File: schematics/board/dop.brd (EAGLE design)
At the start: 65.8 x 65.8 mm, 72 parts

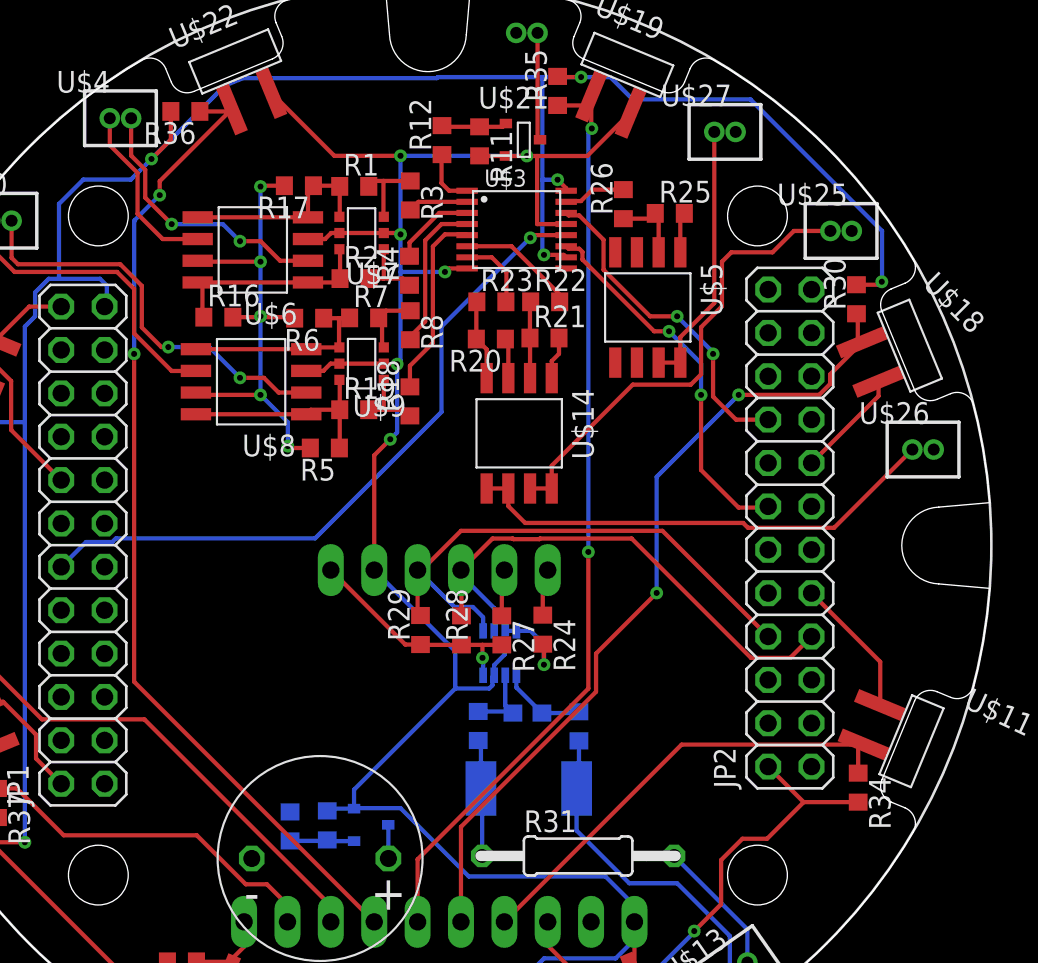
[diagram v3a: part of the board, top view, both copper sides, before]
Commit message: Сделали новую плату для кнопок на нижнем двигателе
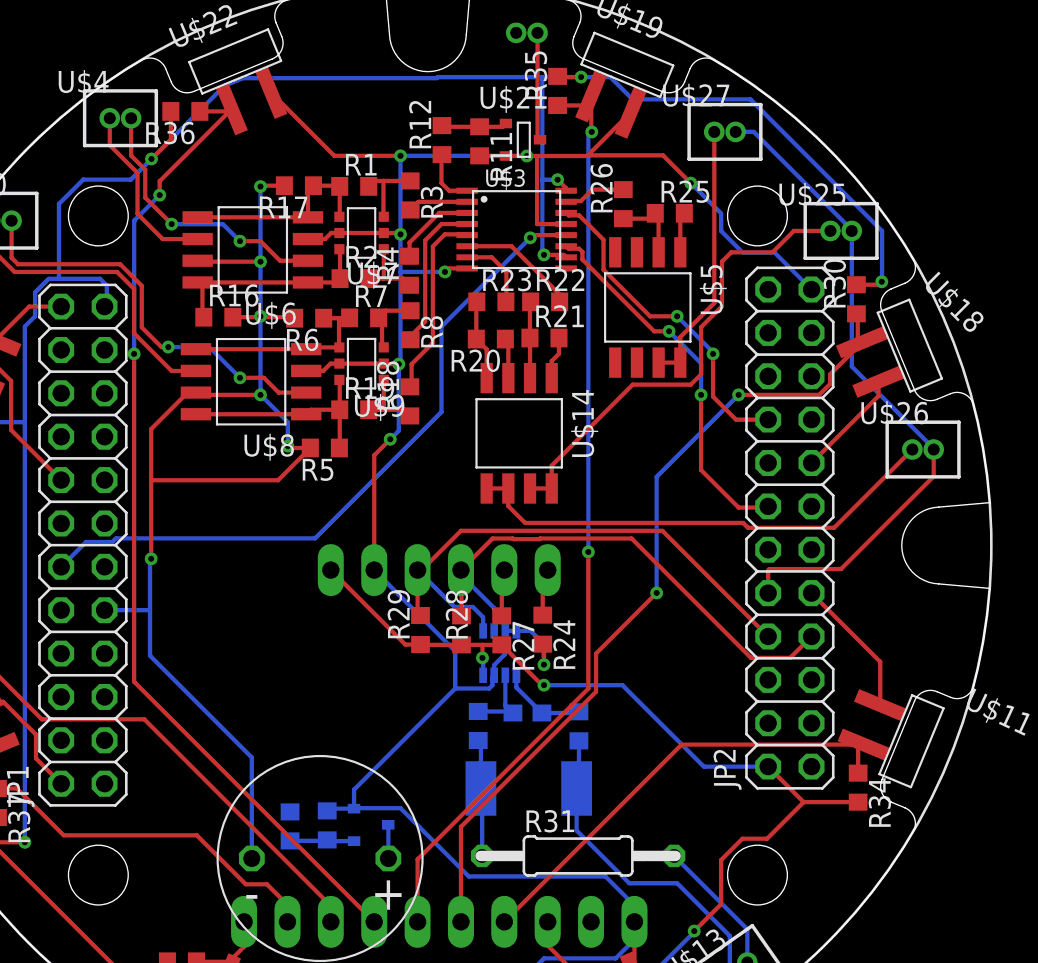
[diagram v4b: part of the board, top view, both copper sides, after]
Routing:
- net 5V: track 30.3 -> 74.2 mm, vias 5 -> 6
- net VAB: track 0.00 -> 38.9 mm
- net 3V3: track 211.5 -> 230.1 mm, vias 12 -> 13
- net GND: track 187.6 -> 204.7 mm, vias 8 -> 9
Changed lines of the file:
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@@
 <?xml version="1.0" encoding="utf-8"?>
 <!DOCTYPE eagle SYSTEM "eagle.dtd">
-<eagle version="9.4.2">
+<eagle version="9.6.2">
 <drawing>
 <settings>
-<setting alwaysvectorfont="yes"/>
+<setting alwaysvectorfont="no"/>
 <setting verticaltext="up"/>
 </settings>
@@
 <via x="31.4" y="51.2" extent="1-16" drill="0.35"/>
 <wire x1="31.4" y1="51.2" x2="31.4" y2="49" width="0.25" layer="16"/>
-<wire x1="31.4" y1="49" x2="31.4" y2="43.8" width="0.25" layer="16"/>
-<wire x1="31.4" y1="43.8" x2="31.2" y2="43.6" width="0.25" layer="16"/>
-<via x="31.2" y="43.6" extent="1-16" drill="0.35"/>
-<wire x1="31.2" y1="43.6" x2="30.45" y2="43.6" width="0.25" layer="1"/>
+<wire x1="31.4" y1="49" x2="31.4" y2="43.6" width="0.25" layer="16"/>
+<wire x1="31.4" y1="43.6" x2="31.3" y2="43.6" width="0.25" layer="16"/>
+<via x="31.3" y="43.6" extent="1-16" drill="0.35"/>
+<wire x1="31.3" y1="43.6" x2="30.45" y2="43.6" width="0.25" layer="1"/>
 <wire x1="30.45" y1="43.6" x2="30.42" y2="43.63" width="0.25" layer="1"/>
 <wire x1="31.4" y1="49" x2="34" y2="49" width="0.25" layer="16"/>
@@
 <via x="31.4" y="55.8" extent="1-16" drill="0.35"/>
 <wire x1="31.4" y1="55.8" x2="31.4" y2="51.2" width="0.25" layer="16"/>
-<wire x1="44.880821875" y1="58.335825" x2="42.334996875" y2="55.79" width="0.25" layer="1"/>
+<wire x1="44.880821875" y1="58.335825" x2="42.372496875" y2="55.8275" width="0.25" layer="1"/>
+<wire x1="42.372496875" y1="55.8275" x2="42.334996875" y2="55.79" width="0.25" layer="1"/>
 <wire x1="42.334996875" y1="55.79" x2="39.4" y2="55.79" width="0.25" layer="1"/>
 <wire x1="39.4" y1="55.79" x2="38.8" y2="55.79" width="0.25" layer="1"/>
@@
 <wire x1="29.86" y1="38.26" x2="30.8" y2="39.2" width="0.25" layer="1"/>
 <via x="30.8" y="39.2" extent="1-16" drill="0.35"/>
-<wire x1="30.8" y1="39.2" x2="31.2" y2="39.6" width="0.25" layer="16"/>
-<wire x1="31.2" y1="39.6" x2="31.2" y2="43.6" width="0.25" layer="16"/>
+<wire x1="30.8" y1="39.2" x2="31.3" y2="39.7" width="0.25" layer="16"/>
+<wire x1="31.3" y1="39.7" x2="31.3" y2="43.6" width="0.25" layer="16"/>
 <wire x1="29.86" y1="31.54" x2="34.605" y2="26.795" width="0.25" layer="16"/>
 <wire x1="34.605" y1="26.795" x2="34.605" y2="24.605" width="0.25" layer="16"/>
@@
 <wire x1="44" y1="8.8" x2="45.1" y2="9.9" width="0.25" layer="16"/>
 <wire x1="45.1" y1="9.9" x2="45.1" y2="10.94" width="0.25" layer="16"/>
+<wire x1="42.372496875" y1="55.8275" x2="46.7725" y2="55.8275" width="0.25" layer="1"/>
+<wire x1="46.7725" y1="55.8275" x2="48.4" y2="54.2" width="0.25" layer="1"/>
+<via x="48.4" y="54.2" extent="1-16" drill="0.35"/>
+<wire x1="48.4" y1="54.2" x2="50.17416875" y2="52.42583125" width="0.25" layer="16"/>
+<wire x1="53.291190625" y1="50.148809375" x2="55.47" y2="47.97" width="0.25" layer="16"/>
+<wire x1="51.421896875" y1="50.148809375" x2="53.291190625" y2="50.148809375" width="0.25" layer="16"/>
+<wire x1="50.17416875" y1="52.42583125" x2="50.17416875" y2="51.3965375" width="0.25" layer="16"/>
+<wire x1="50.17416875" y1="51.3965375" x2="51.421896875" y2="50.148809375" width="0.25" layer="16"/>
+<wire x1="23.828871875" y1="59.492534375" x2="13.46" y2="77" width="0" layer="19" extent="1-1"/>
 <wire x1="59.392534375" y1="42.571125" x2="55.47" y2="47.97" width="0" layer="19" extent="1-1"/>
 <wire x1="55.47" y1="30.19" x2="55.47" y2="37.81" width="0" layer="19" extent="1-1"/>
 <wire x1="55.47" y1="20.03" x2="59.492534375" y2="23.628871875" width="0" layer="19" extent="1-1"/>
-<wire x1="45.1" y1="10.94" x2="55.47" y2="20.03" width="0" layer="19" extent="1-1"/>
 <wire x1="11.53" y1="46.97" x2="25.88" y2="43.205" width="0" layer="19" extent="1-1"/>
 <wire x1="11.53" y1="29.19" x2="11.53" y2="36.81" width="0" layer="19" extent="1-1"/>
 <wire x1="6.6074625" y1="23.428871875" x2="11.53" y2="29.19" width="0" layer="19" extent="1-1"/>
-<wire x1="13.46" y1="77" x2="23.828871875" y2="59.492534375" width="0" layer="19" extent="1-1"/>
 </signal>
 <signal name="N$13">
@@
 <wire x1="25.14" y1="46.35" x2="25.2" y2="46.29" width="0.25" layer="1"/>
 <via x="23.2" y="46.4" extent="1-16" drill="0.35"/>
+<wire x1="22.69" y1="14.65" x2="22.69" y2="20.57" width="0.25" layer="16"/>
+<wire x1="22.69" y1="20.57" x2="16.73" y2="26.53" width="0.25" layer="16"/>
+<wire x1="16.73" y1="26.53" x2="16.73" y2="29.2" width="0.25" layer="16"/>
+<wire x1="16.73" y1="29.2" x2="16.73" y2="32.13" width="0.25" layer="16"/>
+<wire x1="16.73" y1="32.13" x2="16.8" y2="32.2" width="0.25" layer="16"/>
+<via x="16.8" y="32.2" extent="1-16" drill="0.35"/>
+<wire x1="16.8" y1="32.2" x2="16.8" y2="36.8" width="0.25" layer="1"/>
+<wire x1="16.8" y1="39.8" x2="16.8" y2="36.8" width="0.25" layer="1"/>
+<wire x1="18.935" y1="41.935" x2="19.42" y2="41.935" width="0.25" layer="1"/>
+<wire x1="16.8" y1="39.8" x2="18.935" y2="41.935" width="0.25" layer="1"/>
+<wire x1="14.07" y1="29.19" x2="16.72" y2="29.19" width="0.25" layer="16"/>
+<wire x1="16.72" y1="29.19" x2="16.73" y2="29.2" width="0.25" layer="16"/>
+<wire x1="16.8" y1="36.8" x2="24.23" y2="36.8" width="0.25" layer="1"/>
+<wire x1="24.23" y1="36.8" x2="26.12" y2="38.69" width="0.25" layer="1"/>
 <wire x1="23.2" y1="54" x2="18.54" y2="77" width="0" layer="19" extent="1-1"/>
 <wire x1="21.58" y1="46.35" x2="23.2" y2="46.4" width="0" layer="19" extent="1-1"/>
-<wire x1="14.07" y1="29.19" x2="19.42" y2="41.935" width="0" layer="19" extent="1-1"/>
-<wire x1="22.69" y1="14.65" x2="14.07" y2="29.19" width="0" layer="19" extent="1-1"/>
 <wire x1="52.93" y1="37.81" x2="26.12" y2="38.69" width="0" layer="19" extent="1-1"/>
 </signal>
@@
 <wire x1="52.868809375" y1="15.808809375" x2="55.01" y2="17.95" width="0.25" layer="1"/>
 <wire x1="51.421890625" y1="15.808809375" x2="52.868809375" y2="15.808809375" width="0.25" layer="1"/>
+<wire x1="52.93" y1="20.03" x2="49.17" y2="20.03" width="0.25" layer="16"/>
+<wire x1="44.4" y1="24.8" x2="39.8" y2="24.8" width="0.25" layer="16"/>
+<via x="39.8" y="24.8" extent="1-16" drill="0.35"/>
+<wire x1="39.8" y1="24.8" x2="39.69" y2="24.8" width="0.25" layer="1"/>
+<wire x1="39.69" y1="24.8" x2="37.33" y2="27.16" width="0.25" layer="1"/>
+<wire x1="49.17" y1="20.03" x2="44.4" y2="24.8" width="0.25" layer="16"/>
 <wire x1="17.95" y1="58.4" x2="16" y2="77" width="0" layer="19" extent="1-1"/>
-<wire x1="37.33" y1="27.16" x2="52.93" y2="20.03" width="0" layer="19" extent="1-1"/>
 </signal>
 <signal name="N$15">
@@
 <contactref element="U$19" pad="P$1"/>
 <wire x1="42.571125" y1="59.292534375" x2="42.571125" y2="58.8" width="0.25" layer="1"/>
-<wire x1="42.571125" y1="58.8" x2="42.571125" y2="57.428875" width="0.25" layer="1"/>
-<wire x1="42.571125" y1="57.428875" x2="42.6" y2="57.4" width="0.25" layer="1"/>
-<via x="42.6" y="57.4" extent="1-16" drill="0.35"/>
-<wire x1="42.6" y1="57.4" x2="42.4" y2="57.2" width="0.25" layer="16"/>
-<wire x1="42.4" y1="57.2" x2="42.4" y2="32.6" width="0.25" layer="16"/>
+<wire x1="42.571125" y1="58.8" x2="42.571125" y2="57.228875" width="0.25" layer="1"/>
+<wire x1="42.571125" y1="57.228875" x2="42.6" y2="57.2" width="0.25" layer="1"/>
+<via x="42.6" y="57.2" extent="1-16" drill="0.35"/>
+<wire x1="42.6" y1="57.2" x2="42.5" y2="57.2" width="0.25" layer="16"/>
+<wire x1="42.5" y1="57.2" x2="42.4" y2="57.1" width="0.25" layer="16"/>
+<wire x1="42.4" y1="57.1" x2="42.4" y2="32.6" width="0.25" layer="16"/>
 <via x="42.4" y="32.6" extent="1-16" drill="0.35"/>
 <wire x1="42.4" y1="32.6" x2="42.4" y2="24.6" width="0.25" layer="1"/>
@@
 <contactref element="U$3" pad="5"/>
 <wire x1="33.295" y1="50.495" x2="34" y2="51.2" width="0.25" layer="1"/>
-<wire x1="31.95" y1="42.27" x2="31.95" y2="43.50038125" width="0.25" layer="1"/>
-<wire x1="31.95" y1="43.50038125" x2="33.295" y2="44.84538125" width="0.25" layer="1"/>
+<wire x1="32.05" y1="43.60038125" x2="32.05" y2="42.37" width="0.25" layer="1"/>
+<wire x1="31.95" y1="42.27" x2="32.05" y2="42.37" width="0.25" layer="1"/>
+<wire x1="32.05" y1="43.60038125" x2="33.295" y2="44.84538125" width="0.25" layer="1"/>
 <wire x1="33.295" y1="44.84538125" x2="33.295" y2="50.495" width="0.25" layer="1"/>
 <wire x1="34" y1="51.2" x2="35.255" y2="51.2" width="0.25" layer="1"/>
@@
 <contactref element="U$26" pad="3"/>
 <contactref element="U$27" pad="3"/>
+<wire x1="52.93" y1="30.19" x2="52.93" y2="31.53" width="0.25" layer="1"/>
+<wire x1="52.93" y1="31.53" x2="53" y2="31.6" width="0.25" layer="1"/>
+<wire x1="53" y1="31.6" x2="57.2" y2="31.6" width="0.25" layer="1"/>
+<wire x1="57.2" y1="31.6" x2="62.625" y2="37.025" width="0.25" layer="1"/>
+<wire x1="62.625" y1="37.025" x2="62.625" y2="38.6" width="0.25" layer="1"/>
+<wire x1="62.625" y1="38.6" x2="62.304" y2="38.921" width="0.25" layer="16"/>
+<wire x1="62.304" y1="38.921" x2="62.304" y2="38.98480625" width="0.25" layer="16"/>
+<wire x1="57.825" y1="43.46380625" x2="57.825" y2="51.4" width="0.25" layer="16"/>
+<wire x1="62.304" y1="38.98480625" x2="57.825" y2="43.46380625" width="0.25" layer="16"/>
+<wire x1="57.504" y1="51.78480625" x2="57.504" y2="51.721" width="0.25" layer="16"/>
+<wire x1="57.504" y1="51.721" x2="57.825" y2="51.4" width="0.25" layer="16"/>
+<wire x1="51.025" y1="57.2" x2="52.08880625" y2="57.2" width="0.25" layer="16"/>
+<wire x1="52.08880625" y1="57.2" x2="57.504" y2="51.78480625" width="0.25" layer="16"/>
 <wire x1="14.07" y1="36.81" x2="52.93" y2="30.19" width="0" layer="19" extent="1-1"/>
-<wire x1="57.825" y1="51.4" x2="14.07" y2="36.81" width="0" layer="19" extent="1-1"/>
-<wire x1="62.625" y1="38.6" x2="57.825" y2="51.4" width="0" layer="19" extent="1-1"/>
-<wire x1="51.025" y1="57.2" x2="62.625" y2="38.6" width="0" layer="19" extent="1-1"/>
 </signal>
 <signal name="PA6">

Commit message: Начали делать платы СП
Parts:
- removed U$1, U$10, U$25, U$26, U$27, U$4: JST_2CON, CanCubeSat:JST_2CON_1.25
- added ENCODER: JST_3CON, CanCubeSat:JST_3CON_1.25
- added FOTO, MOT1, MOT2, MOT3: JST_2CON, CanCubeSat:JST_2CON_1.25
- added PERE1, PERE2, PERE3: JST-2-2.5, CanCubeSat:JST-2-2.5
- added X1: 53047-02, con-molex:53047-02
- R12: value 100R -> 1k
- moved R36 1.52 mm to (19.4, 57.0), turned to 210 degrees
- moved JP2 1.00 mm to (54.2, 33.0)
- moved R35 0.45 mm to (40.4, 59.2)
- moved R11 0.40 mm to (35.6, 56.6)
- moved R12 0.40 mm to (33.4, 56.7)
- moved U$21 0.40 mm to (38.2, 56.7)
- moved U$2 0.20 mm to (37.2, 26.5)
- renumbered JP3 to POWER, U$12 to PERE-MK, U$13 to SP
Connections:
- new net ENCOD_A: ENCODER.2
- new net ENCOD_B: ENCODER.3
- new net ENCOD_C: ENCODER.1
- new net FOTO_G: FOTO.3
- new net FOTO_R: FOTO.2
- net GND: now also X1.1
- net MOTOR1+: now also MOT1.2; no longer U$10.2
- net MOTOR1-: now also MOT1.3; no longer U$10.3
- net MOTOR2+: now also MOT2.2; no longer U$4.2
- net MOTOR2-: now also MOT2.3; no longer U$4.3
- net MOTOR3-: now also MOT3.3; no longer U$1.3
- net N$17: now also X1.2
- net PERE1_G: now also PERE1.1; no longer U$25.2
- net PERE2_G: now also PERE2.2; no longer U$26.2
- net PERE3_G: now also PERE3.1; no longer U$27.2
- net VAB: now also PERE1.2, PERE2.1, PERE3.2; no longer U$25.3, U$26.3, U$27.3
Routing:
- net VAB: track 38.9 -> 8.12 mm
- net 5V: track 74.2 -> 65.6 mm
- net PERE2_G: track 28.4 -> 20.0 mm
- net N$17: track 3.85 -> 10.6 mm
- net FOTO3: track 48.4 -> 52.3 mm
- net GND: track 204.7 -> 201.7 mm
- net PERE1_G: track 27.8 -> 25.8 mm
- net FOTO5: track 57.7 -> 55.8 mm
- net MOTOR1+: track 18.1 -> 16.2 mm
- net SP+: track 19.1 -> 17.6 mm
- net MOTOR1-: track 24.1 -> 22.7 mm
- net FOTO4: track 54.6 -> 55.9 mm
- net MOTOR3-: track 6.32 -> 7.55 mm
- net FOTO6: track 44.9 -> 43.8 mm
- net MOTOR2+: track 10.4 -> 9.33 mm
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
